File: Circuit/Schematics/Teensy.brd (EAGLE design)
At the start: 127 x 78.7 mm, 36 parts, among them Y1 16 MHz, Y2 32.768 kHz

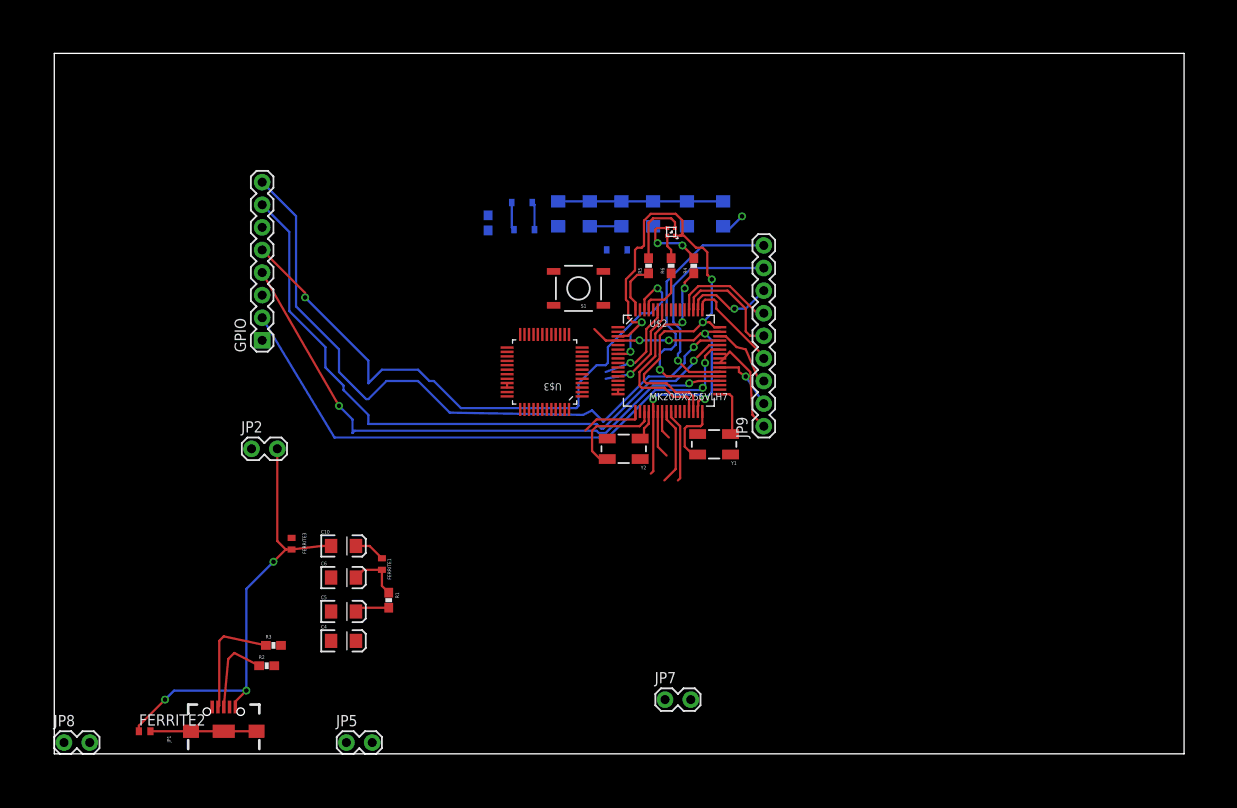
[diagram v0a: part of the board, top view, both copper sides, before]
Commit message: Teensy board designed, redesigning system components board and making hardware components consistent
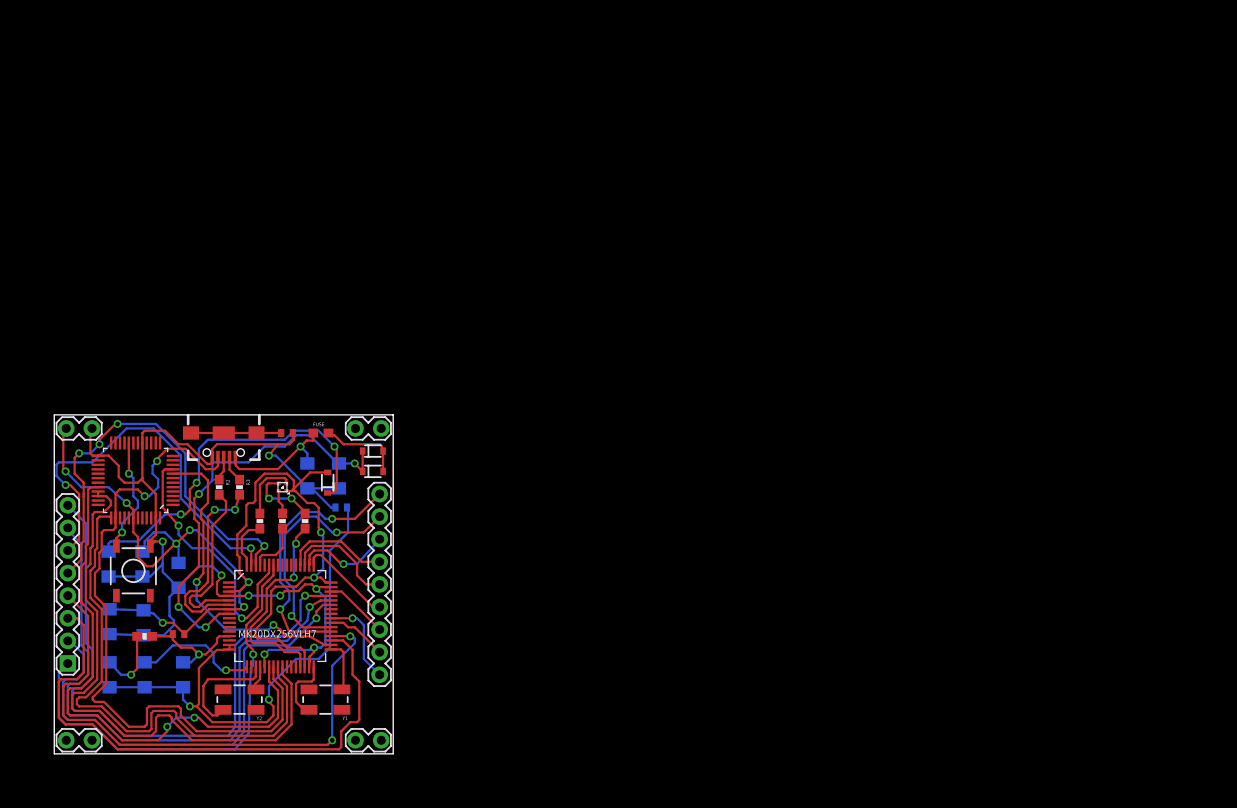
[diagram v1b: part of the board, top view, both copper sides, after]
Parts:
- removed F2: PTC0603, SparkFun-PowerIC:0603
- added FUSE: PTC0603, SparkFun-PowerIC:0603
- C2, C3, C6: value (none) -> 0.1 uF
- moved C9 76.5 mm to (10.0, 14.7), turned to 90 degrees
- moved C2 72.8 mm to (6.10, 21.3), turned to 90 degrees
- moved C8 66.7 mm to (9.91, 21.3), turned to 90 degrees
- moved C7 61.6 mm to (14.0, 20.1), turned to 90 degrees
- moved S1 59.3 mm to (8.89, 20.6), turned to 270 degrees
- moved C3 55.2 mm to (28.4, 31.2), turned to 90 degrees
- moved D1 52.3 mm to (25.7, 30.0)
- moved R4 52.3 mm to (28.2, 26.2)
- moved R5 52.3 mm to (23.1, 26.2)
- moved R6 52.3 mm to (25.7, 26.2)
- moved Y1 52.3 mm to (30.5, 6.10)
- moved U$2 52.3 mm to (25.4, 15.5)
- moved Y2 51.6 mm to (20.8, 6.10)
- moved JP9 51.4 mm to (36.6, 8.89)
- moved U$3 47.6 mm to (9.14, 30.7)
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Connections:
- net N$17 renamed T_TX
- net N$21 renamed CE
- net N$34 renamed SCK
- net N$7 renamed T_RX
- net N$63: now also FUSE.1; no longer F2.1
- net VIN: now also FUSE.2; no longer F2.2
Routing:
- net N$12: track 3.24 -> 77.8 mm, vias 0 -> 2
- net N$31: track 0.00 -> 63.4 mm
- net AGND: track 0.51 -> 59.2 mm, vias 0 -> 2
- net N$13: track 8.78 -> 66.3 mm
- net N$14: track 5.36 -> 62.3 mm, vias 0 -> 2
- net 3.3V: track 70.6 -> 126.5 mm, vias 4 -> 9
- net N$15: track 8.69 -> 60.6 mm
- net N$38: track 0.00 -> 45.4 mm, vias 0 -> 2
- net N$2: track 3.15 -> 47.9 mm, vias 0 -> 4
- net N$9: track 0.00 -> 41.8 mm, vias 0 -> 3
- net N$29: track 11.6 -> 50.8 mm
- net N$11: track 0.00 -> 36.0 mm, vias 0 -> 2
- net N$20: track 0.00 -> 22.3 mm, vias 0 -> 2
- net N$19: track 0.00 -> 19.7 mm
- net N$16: track 10.5 -> 30.0 mm, vias 1 -> 2
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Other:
- board size 127 x 78.7 mm -> 38.1 x 38.1 mm
